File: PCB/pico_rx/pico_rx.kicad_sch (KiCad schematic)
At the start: 0 parts

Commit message: Get CW working
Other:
- added sheet Preamplifier (Preamplifier.kicad_sch)
- sheet Lowpass Filters: file Bandpass.kicad_sch -> Lowpass.kicad_sch
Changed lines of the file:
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@@
 (kicad_sch (version 20230121) (generator eeschema)
   (paper "A4")
-  (sheet (at 74.93 22.86) (size 53.34 52.07) (fields_autoplaced)
+  (sheet (at 129.54 83.82) (size 53.34 52.07) (fields_autoplaced)
     (stroke (width 0.1524) (type solid))
     (fill (color 0 0 0 0.0000))
-    (property "Sheetname" "Quadrature Sampling Detector" (at 74.93 22.1484 0)
+    (property "Sheetname" "Quadrature Sampling Detector" (at 129.54 83.1084 0)
       (effects (font (size 1.27 1.27)) (justify left bottom))
     )
-    (property "Sheetfile" "qsd.kicad_sch" (at 74.93 75.5146 0)
+    (property "Sheetfile" "qsd.kicad_sch" (at 129.54 136.4746 0)
+      (effects (font (size 1.27 1.27)) (justify left top))
+    )
+    (instances
+      (project "pico_rx"
+        (path "/b6f73a49-ac1f-4895-a0f9-8f6954ee587f" (page "4"))
+      )
+    )
+  )
+  (sheet (at 24.13 83.82) (size 46.99 53.34) (fields_autoplaced)
+    (stroke (width 0.1524) (type solid))
+    (fill (color 0 0 0 0.0000))
+    (property "Sheetname" "Preamplifier" (at 24.13 83.1084 0)
+      (effects (font (size 1.27 1.27)) (justify left bottom))
+    )
+    (property "Sheetfile" "Preamplifier.kicad_sch" (at 24.13 137.7446 0)
+      (effects (font (size 1.27 1.27)) (justify left top))
+    )
+    (instances
+      (project "pico_rx"
+        (path "/b6f73a49-ac1f-4895-a0f9-8f6954ee587f" (page "2"))
+      )
+    )
+  )
+  (sheet (at 76.2 83.82) (size 48.26 52.07) (fields_autoplaced)
+    (stroke (width 0.1524) (type solid))
+    (fill (color 0 0 0 0.0000))
+    (property "Sheetname" "Lowpass Filters" (at 76.2 83.1084 0)
+      (effects (font (size 1.27 1.27)) (justify left bottom))
+    )
+    (property "Sheetfile" "Lowpass.kicad_sch" (at 76.2 136.4746 0)
       (effects (font (size 1.27 1.27)) (justify left top))
     )
@@
     )
   )
-  (sheet (at 22.86 22.86) (size 48.26 52.07) (fields_autoplaced)
+  (sheet (at 185.42 82.55) (size 54.61 53.34) (fields_autoplaced)
     (stroke (width 0.1524) (type solid))
     (fill (color 0 0 0 0.0000))
-    (property "Sheetname" "Lowpass Filters" (at 22.86 22.1484 0)
+    (property "Sheetname" "PI Pico" (at 185.42 81.8384 0)
       (effects (font (size 1.27 1.27)) (justify left bottom))
     )
-    (property "Sheetfile" "Bandpass.kicad_sch" (at 22.86 75.5146 0)
+    (property "Sheetfile" "pi_pico.kicad_sch" (at 185.42 136.4746 0)
       (effects (font (size 1.27 1.27)) (justify left top))
     )
     (instances
       (project "pico_rx"
-        (path "/b6f73a49-ac1f-4895-a0f9-8f6954ee587f" (page "2"))
+        (path "/b6f73a49-ac1f-4895-a0f9-8f6954ee587f" (page "5"))
       )
     )
-  )
-  (sheet (at 130.81 22.86) (size 54.61 53.34) (fields_autoplaced)
-    (stroke (width 0.1524) (type solid))
-    (fill (color 0 0 0 0.0000))
-    (property "Sheetname" "PI Pico" (at 130.81 22.1484 0)
-      (effects (font (size 1.27 1.27)) (justify left bottom))
-    )
-    (property "Sheetfile" "pi_pico.kicad_sch" (at 130.81 76.7846 0)
-      (effects (font (size 1.27 1.27)) (justify left top))
-    )
-    (instances
-      (project "pico_rx"
-        (path "/b6f73a49-ac1f-4895-a0f9-8f6954ee587f" (page "4"))
-      )
-    )

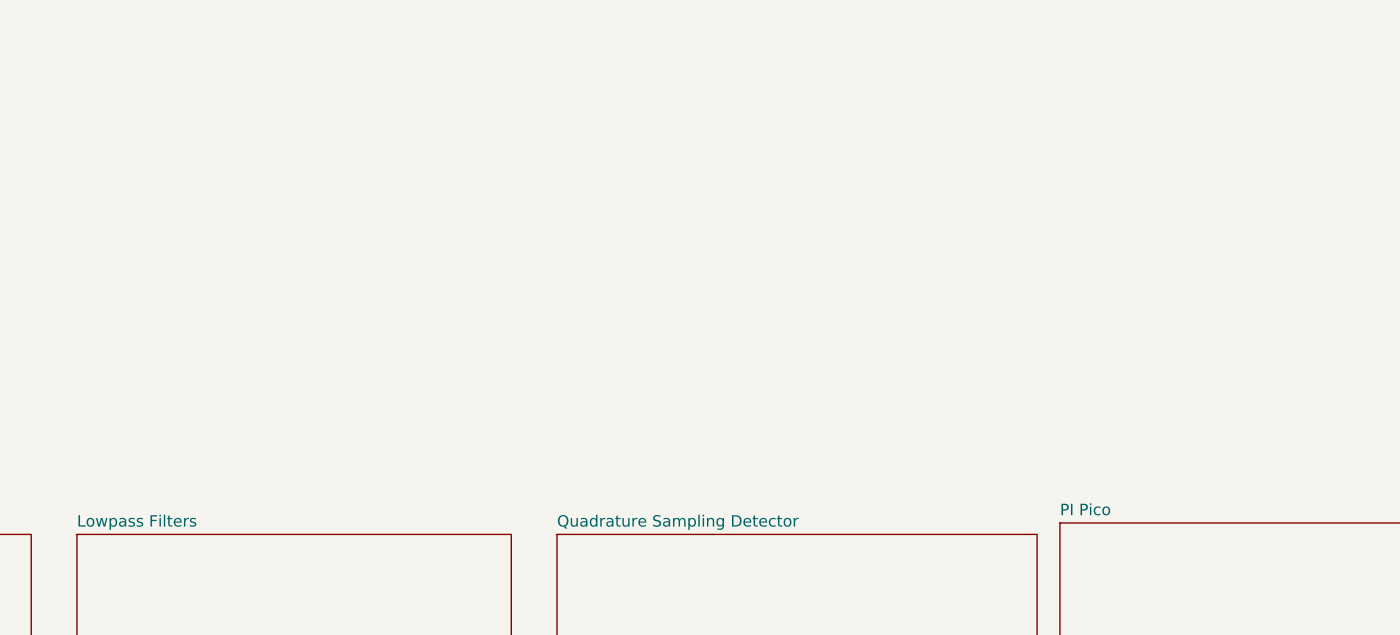
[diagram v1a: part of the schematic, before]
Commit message: Improve frequency resolution by making small adjustments to system clock. Add utility to upload memory contents over USB
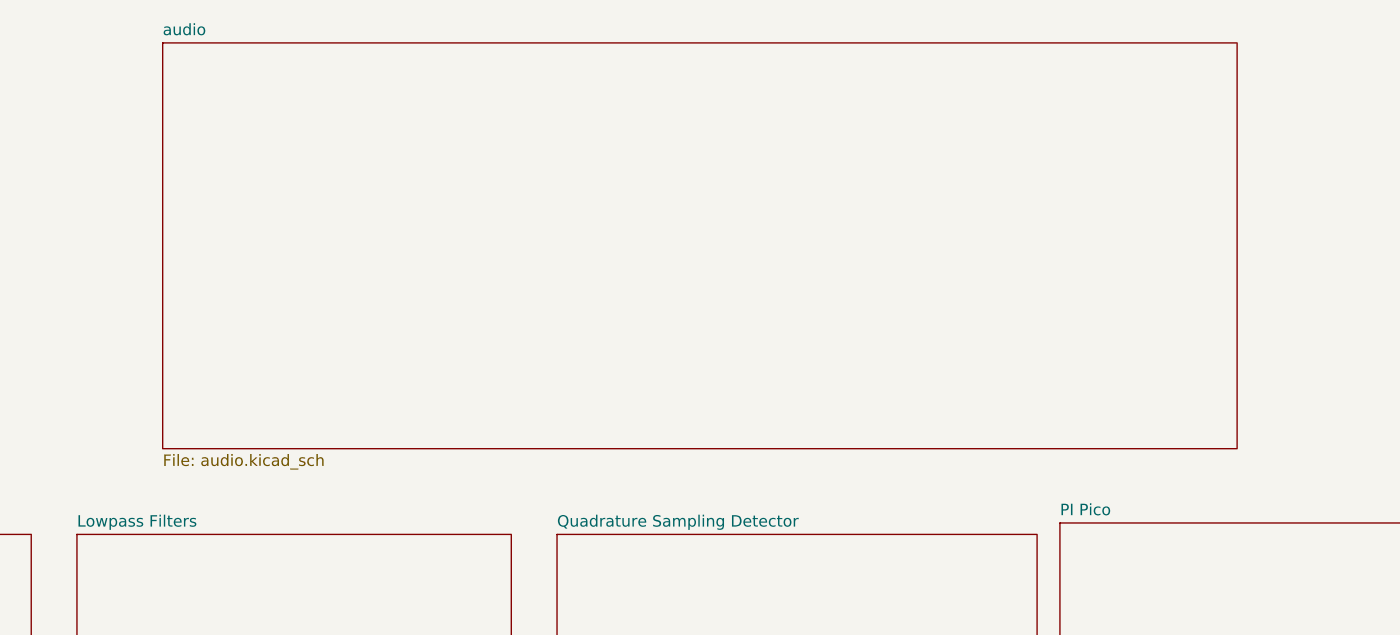
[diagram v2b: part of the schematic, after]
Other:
- added sheet audio (audio.kicad_sch)
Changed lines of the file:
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@@
+    )
+  )
+  (sheet (at 85.725 29.21) (size 119.38 45.085) (fields_autoplaced)
+    (stroke (width 0.1524) (type solid))
+    (fill (color 0 0 0 0.0000))
+    (property "Sheetname" "audio" (at 85.725 28.4984 0)
+      (effects (font (size 1.27 1.27)) (justify left bottom))
+    )
+    (property "Sheetfile" "audio.kicad_sch" (at 85.725 74.8796 0)
+      (effects (font (size 1.27 1.27)) (justify left top))
+    )
+    (instances
+      (project "pico_rx"
+        (path "/b6f73a49-ac1f-4895-a0f9-8f6954ee587f" (page "6"))
+      )
     )
   )

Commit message: Update PCB design to fix issues found
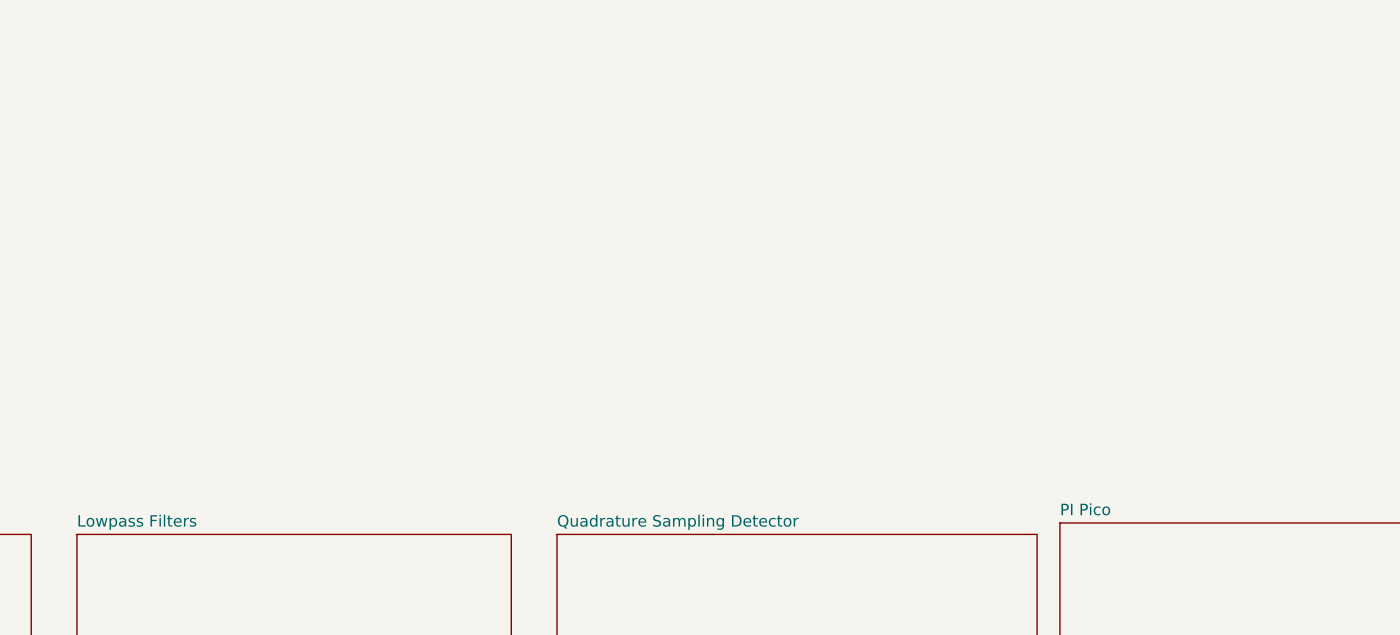
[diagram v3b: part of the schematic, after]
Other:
- removed sheet audio
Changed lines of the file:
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@@
-    )
-  )
-  (sheet (at 85.725 29.21) (size 119.38 45.085) (fields_autoplaced)
-    (stroke (width 0.1524) (type solid))
-    (fill (color 0 0 0 0.0000))
-    (property "Sheetname" "audio" (at 85.725 28.4984 0)
-      (effects (font (size 1.27 1.27)) (justify left bottom))
-    )
-    (property "Sheetfile" "audio.kicad_sch" (at 85.725 74.8796 0)
-      (effects (font (size 1.27 1.27)) (justify left top))
-    )
-    (instances
-      (project "pico_rx"
-        (path "/b6f73a49-ac1f-4895-a0f9-8f6954ee587f" (page "6"))
-      )
     )
   )
